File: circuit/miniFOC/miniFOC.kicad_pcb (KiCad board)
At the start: 2 copper layers, 42 x 26 mm, 79 parts, among them J1 Conn_01x05, J2 Conn_01x03, J3 Conn_01x04, J4 Conn_01x02, J5 Conn_01x01, J6 Conn_01x01, J7 Conn_01x01, Q1 RU30J30M, Q2 RU30J30M, Q3 RU30J30M, U1 XC6206P332MR, U2 CH32V203C8T6, U3 LM321, U4 COS722MR, U5 BDR2L00, U6 BDR2L00, U7 BDR2L00, U8 JW5017S

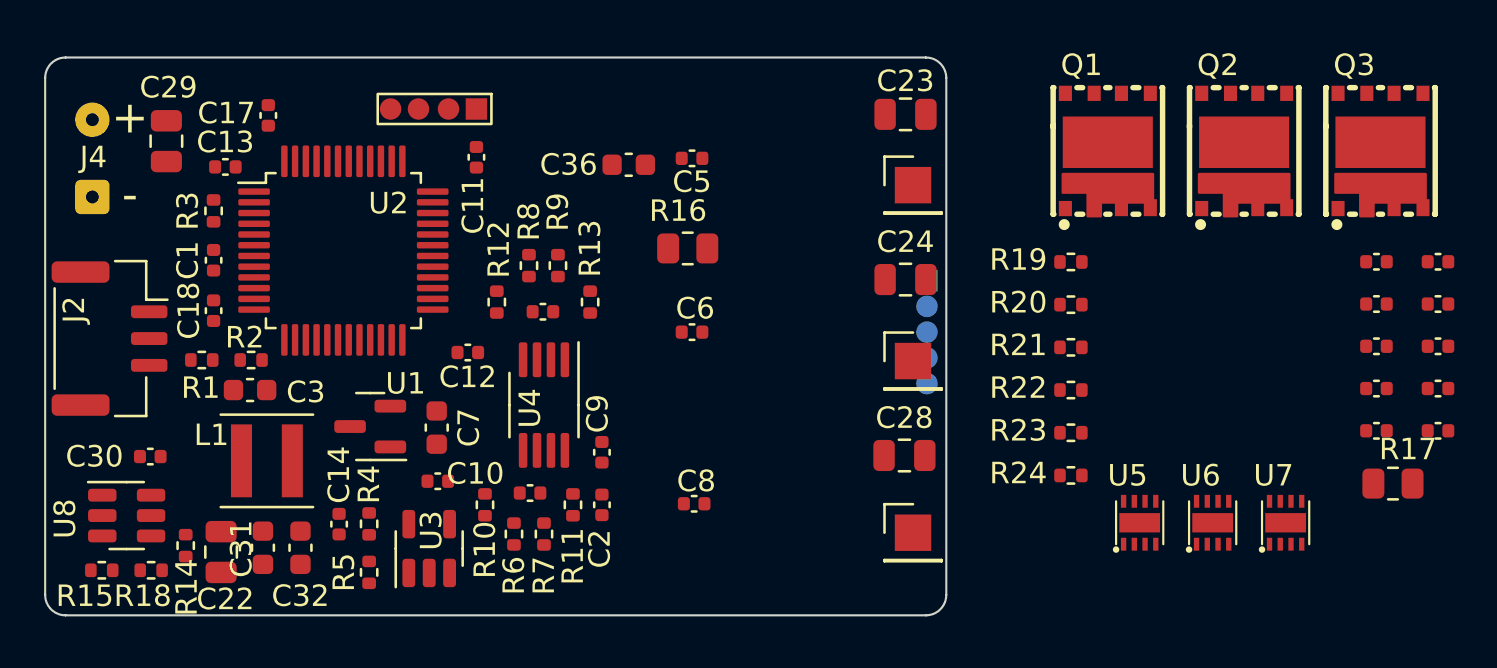
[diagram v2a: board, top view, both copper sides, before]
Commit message: Complete the main circuit design of the second version of miniFOC and remove useless files.
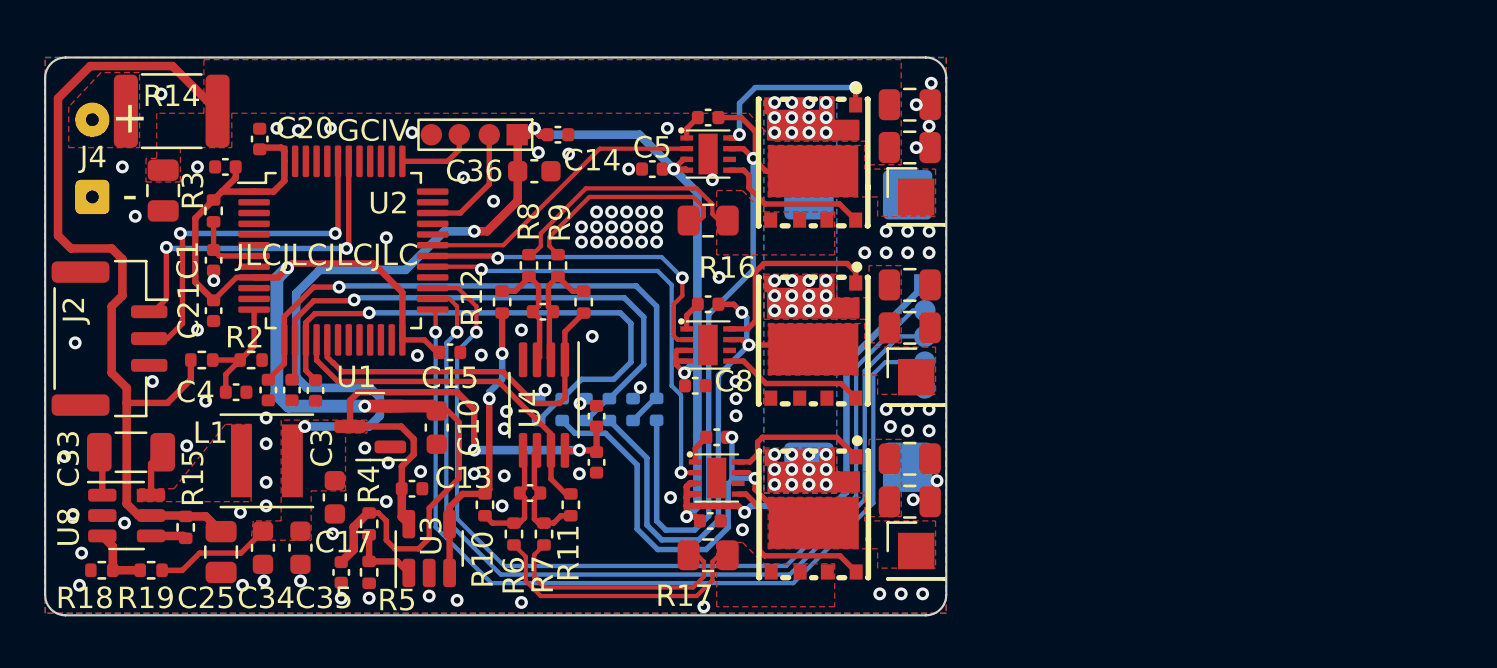
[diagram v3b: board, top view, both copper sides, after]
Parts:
- removed the C19 at (194.8, 103.1)
- removed the C20 at (194.8, 105.1)
- removed the C21 at (194.8, 107.0)
- removed the C33 at (197.6, 105.1)
- removed the C34 at (197.6, 107.0)
- removed the C35 at (197.6, 109.0)
- removed the R19 at (180.5, 101.1)
- added C22: 22uF, library:C_0805_2012Metric, F.Cu at (173.0, 95.8)
- added C23: 22uF, library:C_0805_2012Metric, F.Cu at (173.0, 104.2)
- added C24: 22uF, library:C_0805_2012Metric, F.Cu at (173.0, 112.3)
- added C6: 1uF, library:C_0402_1005Metric, F.Cu at (145.3, 107.1)
- added C7: 1uF, library:C_0402_1005Metric, F.Cu at (144.2, 107.1)
- added C9: 1uF, library:C_0402_1005Metric, F.Cu at (143.1, 107.1)
- added D1: SMAJ18CA, library:D_SMB, B.Cu at (170.6, 98.0)
- added D2: SMAJ18CA, library:D_SMB, B.Cu at (170.6, 110.7)
- added G***: LOGO, library:LOGO, B.Cu at (140.6, 107.7)
- added R14: 0R, library:R_1812_4532Metric, F.Cu at (138.6, 94.1)
- added R25: 1kR, library:R_0402_1005Metric, B.Cu at (155.7, 108.0)
- C33: renamed from C30; footprint library:C_0402_1005Metric -> library:C_1206_3216Metric
- R18: renamed from R15; value 3kR -> 3.9kR
- R19: renamed from R18; value 16kR -> 20kR
- R20, R22, R24: value 1kR -> 10kR; moved to B.Cu
- R21, R23: value 10kR -> 1kR; moved to B.Cu
- moved C4 53.5 mm to (141.6, 107.2)
- moved C28 34.4 mm to (163.6, 94.4)
- moved C30 34.2 mm to (164.0, 109.3)
- moved C29 34.1 mm to (163.6, 103.1)
- moved R17 32.1 mm to (163.6, 114.8), turned to 180 degrees
- moved Q3 31.4 mm to (168.5, 112.9), turned to 180 degrees
- moved U7 26.6 mm to (164.0, 111.2), turned to -90 degrees
- moved U5 26.5 mm to (163.6, 96.1), turned to -90 degrees
- moved U6 24.9 mm to (163.6, 105.0), turned to -90 degrees
- moved R24 23.9 mm to (156.8, 108.0), turned to -90 degrees
- moved R23 22.6 mm to (157.9, 108.0), turned to -90 degrees
- moved Q2 21.9 mm to (168.5, 104.8), turned to 180 degrees
- moved R22 21.5 mm to (159.0, 108.0), turned to -90 degrees
- moved R21 20.6 mm to (160.1, 108.0), turned to -90 degrees
- moved R20 19.9 mm to (161.2, 108.0), turned to -90 degrees
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- renumbered C7 to C10, C8 to C11, C9 to C12, C10 to C13, C11 to C14, C12 to C15, C13 to C16, C14 to C17, C15 to C18, C16 to C19, C17 to C20, C18 to C21, C22 to C25, C23 to C26, C24 to C27, C25 to C28, C26 to C29, C27 to C30, C28 to C31, C29 to C32, C31 to C34, C32 to C35, C6 to C8, R14 to R15
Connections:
- C28 pad 2: /PHASE1 -> /PHASE3
- C30 pad 2: /PHASE3 -> /PHASE1
- J4 pad 2: +15V -> Net-(J4-Pin_2)
- J5 pad 1: /PHASE1 -> /PHASE3
- J7 pad 1: /PHASE3 -> /PHASE1
- Q1 pad 5: /SA1_P -> /SA3_P
- Q1 pad 6: /SA1_P -> /SA3_P
- Q1 pad 7: /SA1_P -> /SA3_P
- Q1 pad 9: /PHASE1 -> /PHASE3
- Q3 pad 5: /SA2_P -> /SA1_P
- Q3 pad 6: /SA2_P -> /SA1_P
- Q3 pad 7: /SA2_P -> /SA1_P
- Q3 pad 9: /PHASE3 -> /PHASE1
- R11 pad 2: /ADC1_CH1 -> /PHASE1_CUR
- R13 pad 2: /ADC1_CH0 -> /PHASE3_CUR
- R16 pad 1: /SA1_P -> /SA3_P
- R17 pad 1: /SA2_P -> /SA1_P
- R20 pad 1: /ADC_U -> /W_VOL
- R20 pad 2: GND -> /PHASE3
- R21 pad 1: /PHASE1 -> GND
- R21 pad 2: /ADC_V -> /W_VOL
- R22 pad 1: /ADC_V -> /V_VOL
- R22 pad 2: GND -> /PHASE2
- R23 pad 1: /PHASE1 -> GND
- R23 pad 2: /ADC_W -> /V_VOL
- R24 pad 1: /ADC_W -> /U_VOL
- R24 pad 2: GND -> /PHASE1
- R6 pad 1: /SA2_P -> /SA1_P
- R8 pad 1: /SA1_P -> /SA3_P
- U2 pad 10: /ADC1_CH0 -> unconnected-(U2-PA0-Pad10)
- U2 pad 11: /ADC1_CH1 -> unconnected-(U2-PA1-Pad11)
- U2 pad 13: /ADC_U -> /W_VOL
- U2 pad 14: /ADC_V -> /V_VOL
- U2 pad 15: /ADC_W -> /U_VOL
- U2 pad 16: unconnected-(U2-PA6-Pad16) -> /PHASE1_CUR
- U2 pad 17: unconnected-(U2-PA7-Pad17) -> /PHASE3_CUR
- U4 pad 1: /ADC1_CH0 -> /PHASE3_CUR
- U4 pad 7: /ADC1_CH1 -> /PHASE1_CUR
- U5 pad 2: /TIM1_CH1 -> /TIM1_CH3
- U5 pad 7: /PHASE1 -> /PHASE3
- U7 pad 2: /TIM1_CH3 -> /TIM1_CH1
- U7 pad 7: /PHASE3 -> /PHASE1
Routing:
- net +5V: track 0.00 -> 111.5 mm, vias 0 -> 9
- net +3.3V: track 0.00 -> 55.7 mm, vias 0 -> 2
- net /SPI_MISO: track 0.00 -> 43.8 mm, vias 0 -> 1
- net /SPI_CLK: track 0.00 -> 42.9 mm, vias 0 -> 1
- net /SPI_CS: track 0.00 -> 41.9 mm, vias 0 -> 1
- net +15V: track 0.00 -> 40.0 mm, vias 0 -> 36
- net /PHASE3: track 0.00 -> 32.8 mm, vias 0 -> 1
- net /W_VOL: track 0.00 -> 27.4 mm, vias 0 -> 1
- net /V_VOL: track 0.00 -> 25.9 mm, vias 0 -> 1
- net /U_VOL: track 0.00 -> 25.6 mm, vias 0 -> 1
- net /PHASE2: track 0.00 -> 25.3 mm, vias 0 -> 2
- net /PHASE1: track 0.00 -> 22.6 mm, vias 0 -> 2
- net GND: track 0.00 -> 21.9 mm, vias 0 -> 104
- net /TIM1_CH1: track 0.00 -> 21.1 mm, vias 0 -> 2
- net /PHASE3_CUR: track 0.00 -> 17.2 mm
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- added copper zone on B.Cu, net +15V
- added copper zone on F.Cu, net +15V
- added copper zone on F.Cu, net +5V
- added copper zone on F.Cu, net /PHASE1
- added copper zone on F.Cu, net /PHASE2
- added copper zone on F.Cu, net /PHASE3
- added copper zone on F.Cu, net /SA1_P
- added copper zone on F.Cu, net /SA3_P
- added copper zone on B.Cu, net GND
- added copper zone on F.Cu, net GND
- added copper zone on F.Cu, net Net-(J4-Pin_2)
- added copper zone on F.Cu, net Net-(U8-SW)
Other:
- rule pad_to_mask_clearance: 0 -> 0.1
- board text added: "GCIV"
- board text added: "JLCJLCJLCJLC"
- board text added: "VICEG"
- board text added: "www.github.com/zhuyanzhen1/miniFOC"
- board text removed: "V I C E G"

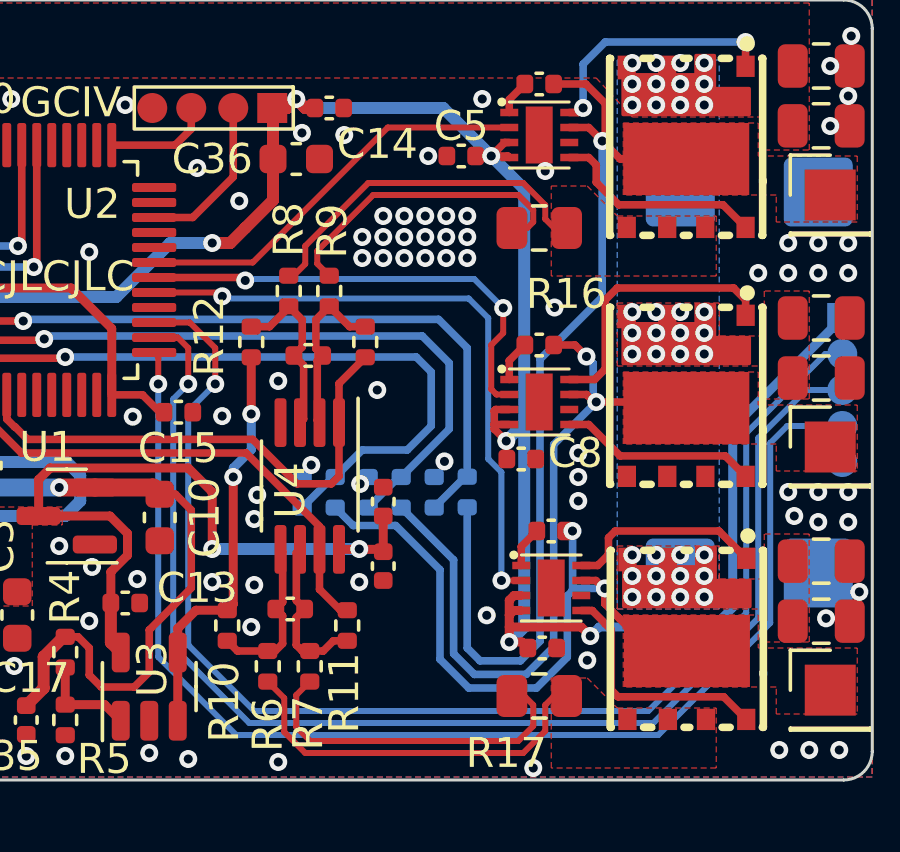
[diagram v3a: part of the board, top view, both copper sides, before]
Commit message: Modify the sampling resistor package in the schematic diagram and PCB, and change its resistance value to 5 milliohms to adapt to the current sampling range of 20A.
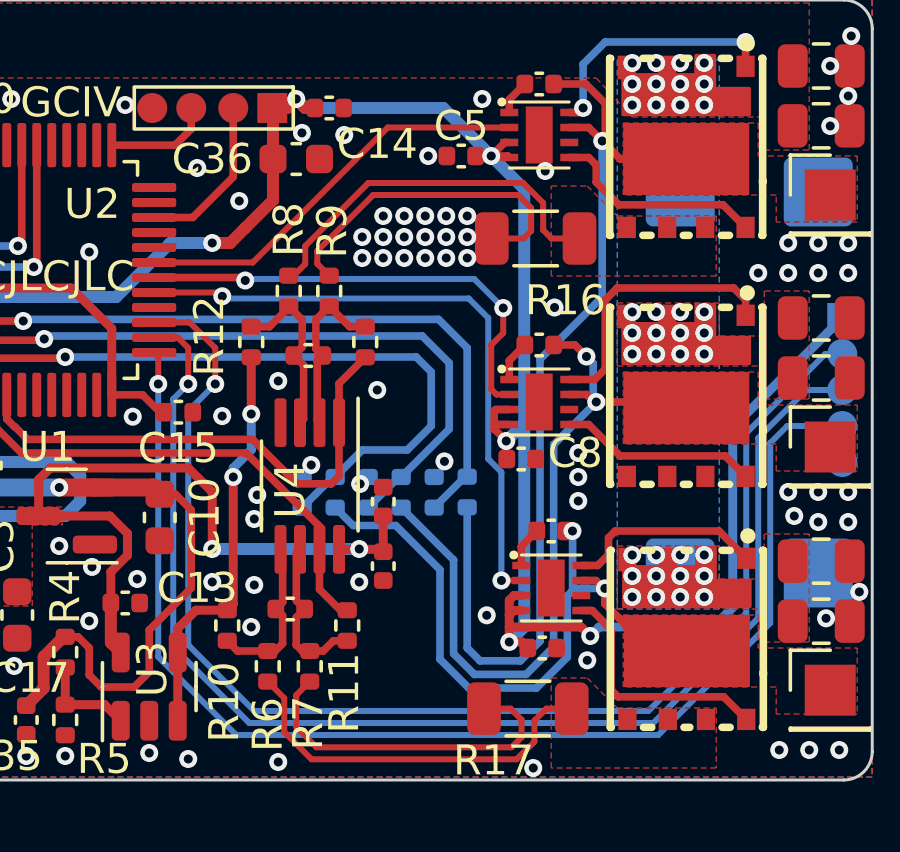
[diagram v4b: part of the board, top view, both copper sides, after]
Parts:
- R16, R17: value 20mR -> 5mR; footprint library:R_0805_2012Metric -> library:R_1206_3216Metric
- moved R17 0.57 mm to (163.2, 115.2)
- moved R16 0.37 mm to (163.5, 99.5)
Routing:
- net GND: track 21.9 -> 22.9 mm
- net /SA3_P: track 11.8 -> 12.6 mm

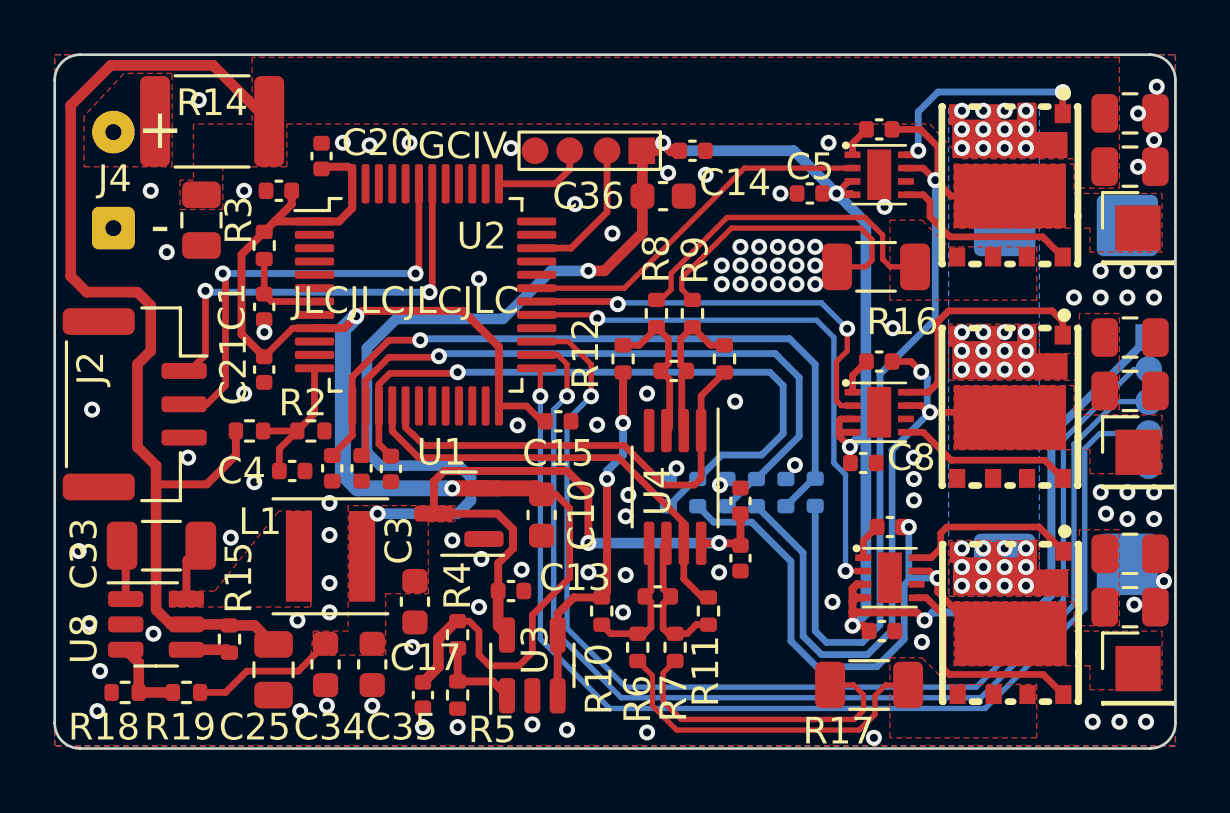
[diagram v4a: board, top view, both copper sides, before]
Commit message: Updated PCB and schematic libraries to add buffer capacitors for current sampling.
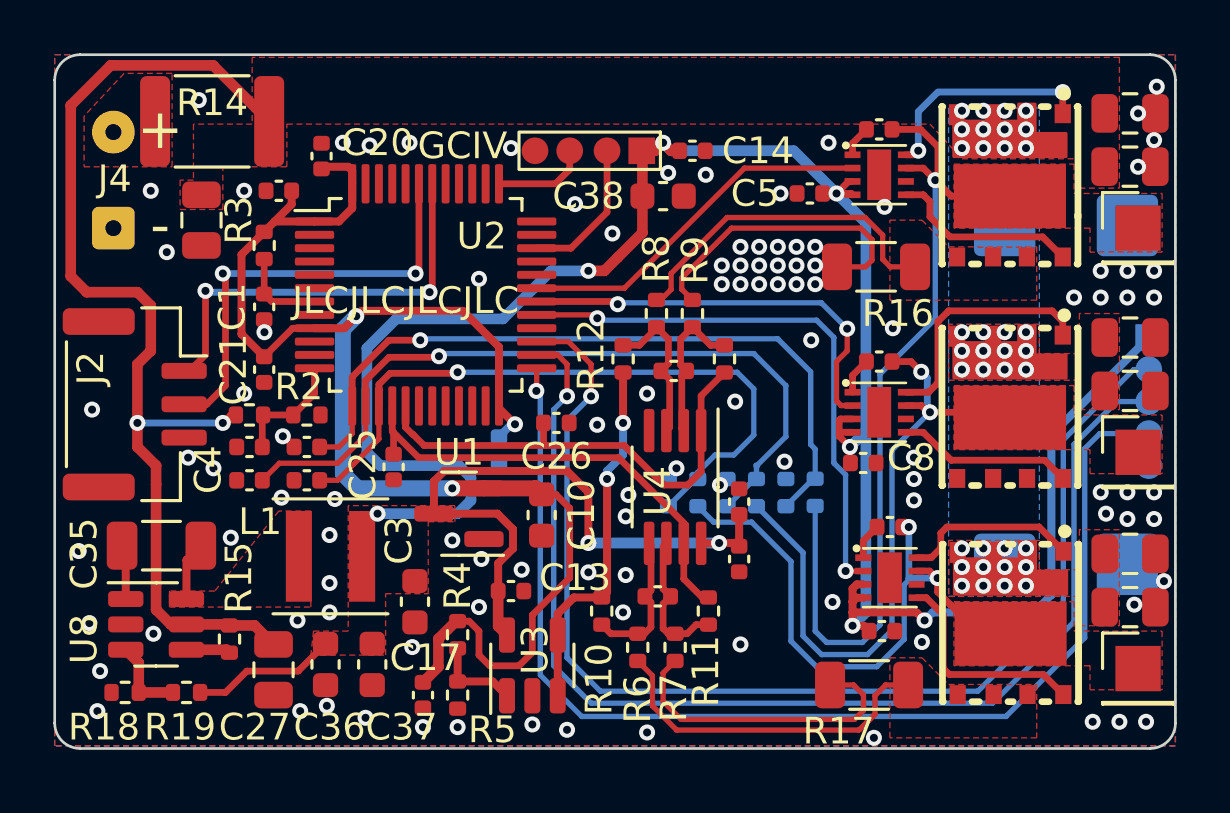
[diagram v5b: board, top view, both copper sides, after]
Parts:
- added C25: 1uF, library:C_0402_1005Metric, F.Cu at (145.4, 107.0)
- added C26: 1uF, library:C_0402_1005Metric, F.Cu at (151.5, 105.4)
- C15: moved to B.Cu
- C6, C7, C9: value 1uF -> 100nF
- R1, R20, R22, R24: value 10kR -> 1kR
- R2, R21, R23, R25: value 1kR -> 160R
- moved C7 4.22 mm to (140.0, 107.5), turned to 180 degrees
- moved C6 3.18 mm to (142.2, 107.5), turned to 180 degrees
- moved C15 2.46 mm to (149.3, 106.4), turned to -90 degrees
- moved C4 1.84 mm to (140.0, 106.3), turned to 180 degrees
- moved C9 1.24 mm to (142.2, 106.3), turned to 180 degrees
- moved R2 0.62 mm to (142.2, 105.1)
- moved R1 0.60 mm to (140.0, 105.1)
- moved C12 0.06 mm to (158.3, 108.3)
- moved C2 0.06 mm to (158.3, 110.5)
- renumbered C25 to C27, C26 to C28, C27 to C29, C28 to C30, C29 to C31, C30 to C32, C31 to C33, C32 to C34, C33 to C35, C34 to C36, C35 to C37, C36 to C38
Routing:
- net /V_VOL: track 25.9 -> 28.8 mm
- net /SPI_CS: track 41.9 -> 43.5 mm
- net /SPI_CLK: track 42.9 -> 44.2 mm
- net /ADC1_CH2: track 5.68 -> 4.42 mm
- net /SPI_MISO: track 43.8 -> 44.7 mm
- net /PHASE1_CUR: track 16.6 -> 17.5 mm
- net /PHASE3_CUR: track 17.2 -> 17.9 mm
- net +15V: track 40.0 -> 39.4 mm, vias 36 -> 38
- net +3.3V: track 55.7 -> 55.4 mm, vias 2 -> 3
- net GND: vias 104 -> 106
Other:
- board text added: "Version 2.0.2"
